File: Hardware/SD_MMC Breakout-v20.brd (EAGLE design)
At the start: 39.4 x 33 mm, 8 parts, among them U1 SD_CARD_SOCKET4UCON

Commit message: Added standoffs, sch work
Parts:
- added FRAME1: FRAME-LETTER, SparkFun-Aesthetics:CREATIVE_COMMONS
- added U$4, U$5: (no value), SparkFun-Electromechanical:STAND-OFF-TIGHT
- U$2: device SparkFun-Aesthetics:CREATIVE_COMMONS -> SparkFun-Aesthetics:CREATIVE_COMMONS@1
- moved JP2 17.8 mm to (19.1, 0.00)
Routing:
- net D2: track 8.53 -> 9.15 mm
- net D3: track 8.53 -> 9.11 mm
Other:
- board size 39.4 x 33 mm -> 39.4 x 35.6 mm
- board text added: "A. Weiss"
- board text added: "Revised by: Patrick Alberts"
- board text added: "v21"
- board text removed: "v20"
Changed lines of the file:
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@@
 <?xml version="1.0" encoding="utf-8"?>
 <!DOCTYPE eagle SYSTEM "eagle.dtd">
-<eagle version="6.4">
+<eagle version="6.5.0">
 <drawing>
 <settings>
@@
 <layer number="106" name="bPlate" color="7" fill="1" visible="no" active="yes"/>
 <layer number="107" name="Crop" color="7" fill="1" visible="no" active="yes"/>
+<layer number="108" name="tplace-old" color="10" fill="1" visible="yes" active="yes"/>
+<layer number="109" name="ref-old" color="11" fill="1" visible="yes" active="yes"/>
 <layer number="116" name="Patch_BOT" color="9" fill="4" visible="no" active="yes"/>
 <layer number="121" name="_tsilk" color="7" fill="1" visible="no" active="yes"/>
@@
 <layer number="144" name="Drill_legend" color="7" fill="1" visible="no" active="yes"/>
 <layer number="151" name="HeatSink" color="7" fill="1" visible="no" active="yes"/>
+<layer number="199" name="Contour" color="7" fill="1" visible="yes" active="yes"/>
 <layer number="200" name="200bmp" color="1" fill="10" visible="no" active="no"/>
 <layer number="201" name="201bmp" color="2" fill="1" visible="no" active="no"/>
@@
 <board>
 <plain>
-<wire x1="0" y1="0" x2="39.37" y2="0" width="0.2032" layer="20"/>
-<wire x1="39.37" y1="0" x2="39.37" y2="33.02" width="0.2032" layer="20"/>
-<wire x1="39.37" y1="33.02" x2="0" y2="33.02" width="0.2032" layer="20"/>
-<wire x1="0" y1="33.02" x2="0" y2="0" width="0.2032" layer="20"/>
+<wire x1="0" y1="-1.27" x2="39.37" y2="-1.27" width="0.2032" layer="20"/>
+<wire x1="39.37" y1="-1.27" x2="39.37" y2="34.29" width="0.2032" layer="20"/>
+<wire x1="39.37" y1="34.29" x2="0" y2="34.29" width="0.2032" layer="20"/>
+<wire x1="0" y1="34.29" x2="0" y2="-1.27" width="0.2032" layer="20"/>
 <text x="2.921" y="14.732" size="1.016" layer="21" ratio="20">VCC</text>
 <text x="38.1" y="10.922" size="1.778" layer="21" ratio="20" rot="R90">SD/MMC</text>
-<text x="38.227" y="19.304" size="1.778" layer="16" font="vector" ratio="15" rot="MR270">v20</text>
+<text x="38.227" y="19.304" size="1.778" layer="16" font="vector" ratio="15" rot="MR270">v21</text>
 <text x="2.921" y="12.192" size="1.016" layer="21" ratio="20">GND</text>
 <text x="2.921" y="9.652" size="1.016" layer="21" ratio="20">D0</text>
@@
 <text x="2.921" y="27.432" size="1.016" layer="21" ratio="20">D2</text>
 <text x="2.921" y="4.572" size="1.016" layer="21" ratio="20">WP</text>
+<text x="24.892" y="-14.351" size="1.778" layer="51">A. Weiss</text>
+<text x="10.287" y="-17.018" size="1.778" layer="51">Revised by: Patrick Alberts</text>
 </plain>
 <attributes>
@@
 <element name="U1" library="SparkFun-Connectors" package="SDCARD_4UCONN" value="SD_CARD_SOCKET4UCON" x="10.16" y="16.51"/>
 <element name="JP1" library="SparkFun-Connectors" package="1X12_HOLES_ONLY" value="M12POGOPIN_HOLES_ONLY" x="6.858" y="2.54" rot="MR90"/>
-<element name="U$2" library="SparkFun-Aesthetics" package="CREATIVE_COMMONS" value="CREATIVE_COMMONS" x="19.05" y="-8.89"/>
+<element name="U$2" library="SparkFun-Aesthetics" package="CREATIVE_COMMONS@1" value="CREATIVE_COMMONS" x="19.05" y="-8.89"/>
 <element name="U$3" library="SparkFun-Aesthetics" package="OSHW-LOGO-S" value="OSHW-LOGOS" x="17.78" y="16.51" rot="MR90"/>
 <element name="JP5" library="SparkFun-Connectors" package="1X10" value="M10&quot;" x="1.27" y="5.08" rot="R90"/>
-<element name="JP2" library="SparkFun" package="MICRO-FIDUCIAL" value="FIDUCIALUFIDUCIAL" x="1.27" y="1.27"/>
+<element name="JP2" library="SparkFun" package="MICRO-FIDUCIAL" value="FIDUCIALUFIDUCIAL" x="19.05" y="0"/>
 <element name="JP3" library="SparkFun" package="MICRO-FIDUCIAL" value="FIDUCIALUFIDUCIAL" x="38.1" y="31.75"/>
+<element name="U$4" library="SparkFun-Electromechanical" package="STAND-OFF-TIGHT" value="" x="2.54" y="31.75"/>
+<element name="U$5" library="SparkFun-Electromechanical" package="STAND-OFF-TIGHT" value="" x="2.54" y="1.27"/>
+<element name="FRAME1" library="SparkFun-Aesthetics" package="CREATIVE_COMMONS" value="FRAME-LETTER" x="-1.50375625" y="-13.97"/>
 </elements>
 <signals>
@@
 <contactref element="U1" pad="3"/>
 <polygon width="0.254" layer="16" isolate="0.3048">
-<vertex x="0" y="33.02"/>
-<vertex x="0" y="0"/>
-<vertex x="39.37" y="0"/>
-<vertex x="39.37" y="33.02"/>
+<vertex x="0" y="34.29"/>
+<vertex x="0" y="-1.27"/>
+<vertex x="39.37" y="-1.27"/>
+<vertex x="39.37" y="34.29"/>
 </polygon>
 <polygon width="0.254" layer="1" isolate="0.3048">
-<vertex x="0" y="33.02"/>
-<vertex x="0" y="0"/>
-<vertex x="39.37" y="0"/>
-<vertex x="39.37" y="33.02"/>
+<vertex x="0" y="34.29"/>
+<vertex x="0" y="-1.27"/>
+<vertex x="39.37" y="-1.27"/>
+<vertex x="39.37" y="34.29"/>
 </polygon>
 <contactref element="U1" pad="6"/>
@@
 <contactref element="U1" pad="9"/>
 <wire x1="9.16" y1="26.4" x2="8.89" y2="26.67" width="0.254" layer="1"/>
-<wire x1="8.89" y1="26.67" x2="3.81" y2="26.67" width="0.254" layer="1"/>
-<wire x1="3.81" y1="26.67" x2="2.54" y2="26.67" width="0.254" layer="1"/>
+<wire x1="8.89" y1="26.67" x2="2.54" y2="26.67" width="0.254" layer="1"/>
 <contactref element="JP5" pad="10"/>
 <wire x1="2.54" y1="26.67" x2="1.27" y2="27.94" width="0.254" layer="1"/>
-<wire x1="9.16" y1="26.4" x2="9.16" y2="25.78" width="0" layer="19" extent="1-1"/>
+<wire x1="9.16" y1="26.4" x2="9.16" y2="25.78" width="0.254" layer="1"/>
 </signal>
 <signal name="D3">
@@
 <wire x1="8.89" y1="24.13" x2="2.54" y2="24.13" width="0.254" layer="1"/>
 <wire x1="2.54" y1="24.13" x2="1.27" y2="25.4" width="0.254" layer="1"/>
-<wire x1="9.16" y1="23.86" x2="9.16" y2="23.28" width="0" layer="19" extent="1-1"/>
+<wire x1="9.16" y1="23.86" x2="9.16" y2="23.28" width="0.254" layer="1"/>
 </signal>
 </signals>

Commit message: Updated Sch
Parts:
- removed U$2: CREATIVE_COMMONS, SparkFun-Aesthetics:CREATIVE_COMMONS@1
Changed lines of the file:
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@@
 <element name="U1" library="SparkFun-Connectors" package="SDCARD_4UCONN" value="SD_CARD_SOCKET4UCON" x="10.16" y="16.51"/>
 <element name="JP1" library="SparkFun-Connectors" package="1X12_HOLES_ONLY" value="M12POGOPIN_HOLES_ONLY" x="6.858" y="2.54" rot="MR90"/>
-<element name="U$2" library="SparkFun-Aesthetics" package="CREATIVE_COMMONS@1" value="CREATIVE_COMMONS" x="19.05" y="-8.89"/>
 <element name="U$3" library="SparkFun-Aesthetics" package="OSHW-LOGO-S" value="OSHW-LOGOS" x="17.78" y="16.51" rot="MR90"/>
 <element name="JP5" library="SparkFun-Connectors" package="1X10" value="M10&quot;" x="1.27" y="5.08" rot="R90"/>

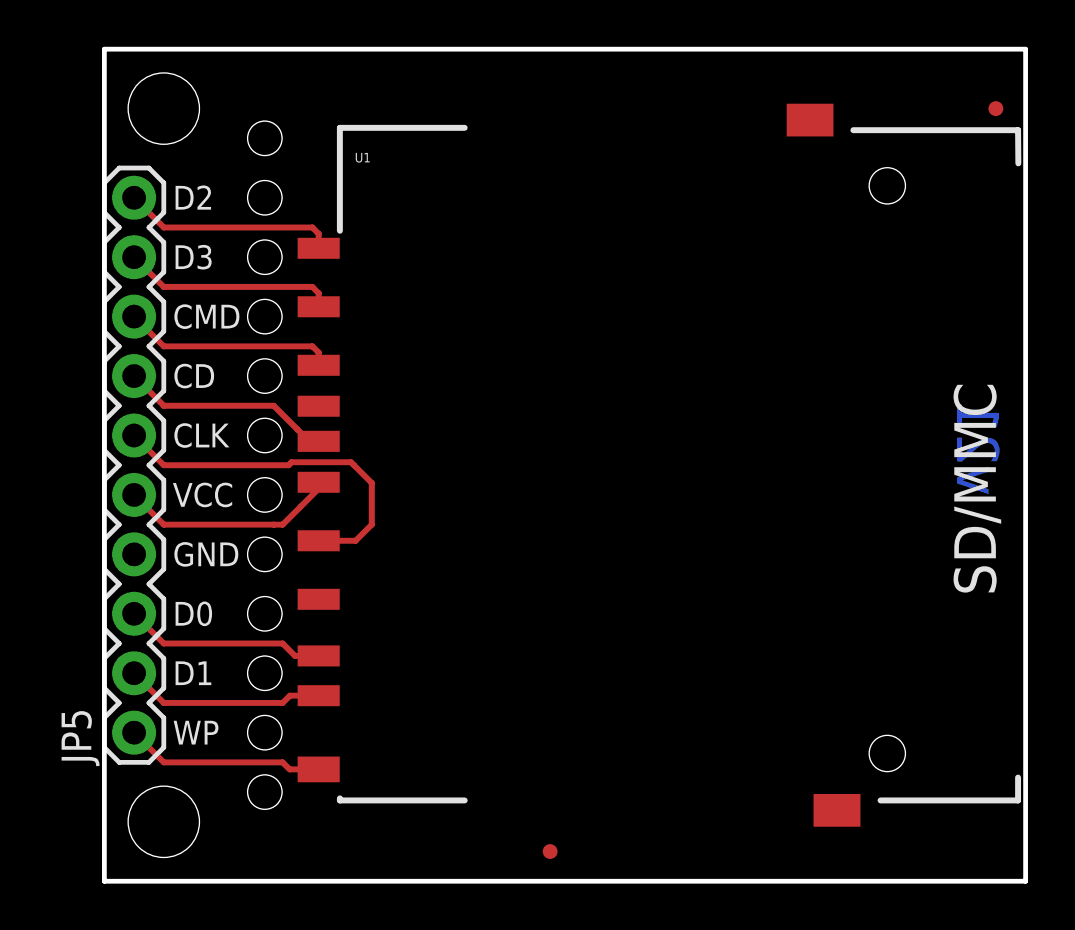
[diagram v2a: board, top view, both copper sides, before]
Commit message: added new sd socket
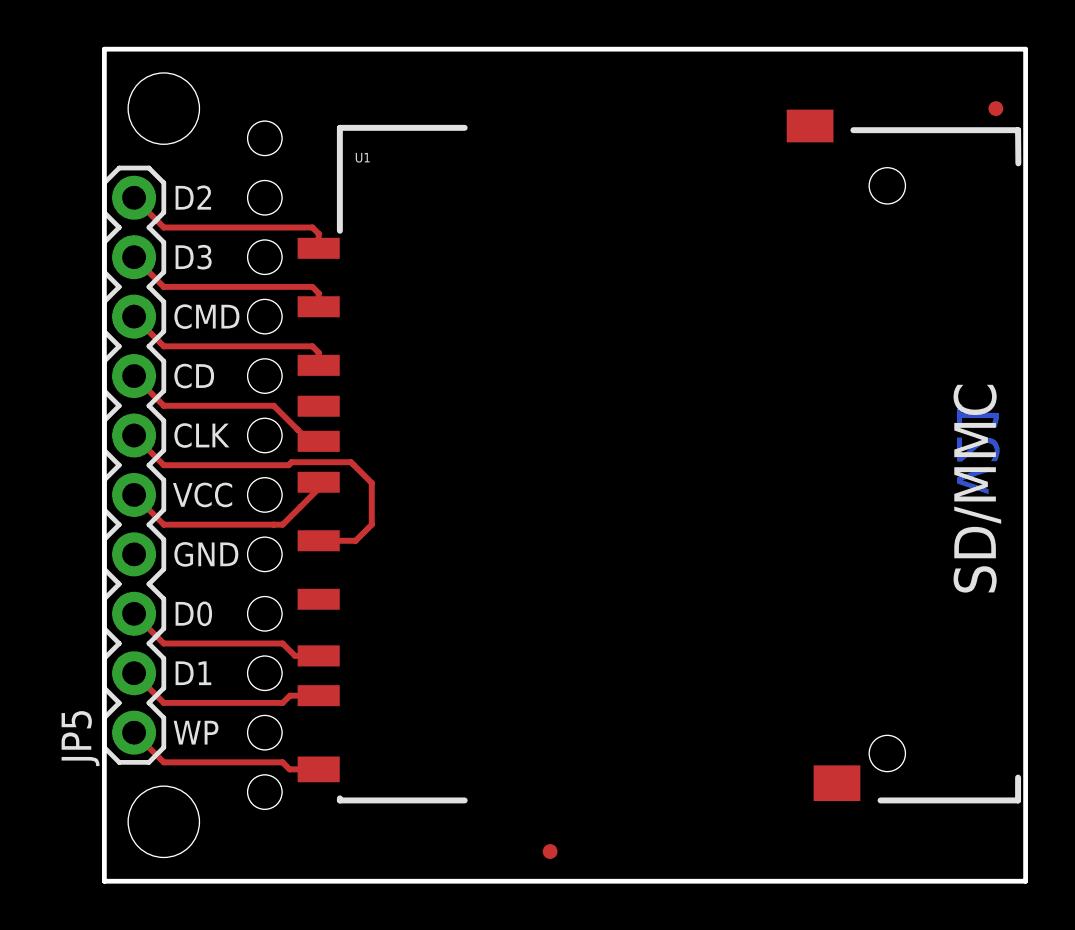
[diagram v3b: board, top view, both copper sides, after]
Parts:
- U1: value SD_CARD_SOCKET4UCON -> SD_CARD_SOCKET; device SparkFun-Connectors:SDCARD_4UCONN -> SparkFun-Connectors:SD_1:1
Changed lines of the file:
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@@
 <?xml version="1.0" encoding="utf-8"?>
 <!DOCTYPE eagle SYSTEM "eagle.dtd">
-<eagle version="6.5.0">
+<eagle version="6.4">
 <drawing>
 <settings>
@@
 <layer number="18" name="Vias" color="2" fill="1" visible="yes" active="yes"/>
 <layer number="19" name="Unrouted" color="6" fill="1" visible="yes" active="yes"/>
-<layer number="20" name="Dimension" color="6" fill="1" visible="yes" active="yes"/>
+<layer number="20" name="Dimension" color="15" fill="1" visible="yes" active="yes"/>
 <layer number="21" name="tPlace" color="16" fill="1" visible="yes" active="yes"/>
 <layer number="22" name="bPlace" color="14" fill="1" visible="yes" active="yes"/>
@@
 <layer number="106" name="bPlate" color="7" fill="1" visible="no" active="yes"/>
 <layer number="107" name="Crop" color="7" fill="1" visible="no" active="yes"/>
-<layer number="108" name="tplace-old" color="10" fill="1" visible="yes" active="yes"/>
-<layer number="109" name="ref-old" color="11" fill="1" visible="yes" active="yes"/>
+<layer number="108" name="tplace-old" color="10" fill="1" visible="no" active="yes"/>
+<layer number="109" name="ref-old" color="11" fill="1" visible="no" active="yes"/>
+<layer number="110" name="fp0" color="7" fill="1" visible="yes" active="yes"/>
+<layer number="111" name="LPC17xx" color="7" fill="1" visible="yes" active="yes"/>
+<layer number="112" name="tSilk" color="7" fill="1" visible="yes" active="yes"/>
+<layer number="113" name="IDFDebug" color="4" fill="1" visible="yes" active="yes"/>
 <layer number="116" name="Patch_BOT" color="9" fill="4" visible="no" active="yes"/>
 <layer number="121" name="_tsilk" color="7" fill="1" visible="no" active="yes"/>
 <layer number="122" name="_bsilk" color="7" fill="1" visible="no" active="yes"/>
+<layer number="123" name="tTestmark" color="7" fill="1" visible="yes" active="yes"/>
+<layer number="124" name="bTestmark" color="7" fill="1" visible="yes" active="yes"/>
 <layer number="125" name="_tNames" color="7" fill="1" visible="no" active="yes"/>
+<layer number="126" name="_bNames" color="7" fill="1" visible="yes" active="yes"/>
+<layer number="127" name="_tValues" color="7" fill="1" visible="yes" active="yes"/>
+<layer number="128" name="_bValues" color="7" fill="1" visible="yes" active="yes"/>
+<layer number="131" name="tAdjust" color="7" fill="1" visible="yes" active="yes"/>
+<layer number="132" name="bAdjust" color="7" fill="1" visible="yes" active="yes"/>
 <layer number="144" name="Drill_legend" color="7" fill="1" visible="no" active="yes"/>
 <layer number="151" name="HeatSink" color="7" fill="1" visible="no" active="yes"/>
-<layer number="199" name="Contour" color="7" fill="1" visible="yes" active="yes"/>
+<layer number="152" name="_bDocu" color="7" fill="1" visible="yes" active="yes"/>
+<layer number="199" name="Contour" color="7" fill="1" visible="no" active="yes"/>
 <layer number="200" name="200bmp" color="1" fill="10" visible="no" active="no"/>
 <layer number="201" name="201bmp" color="2" fill="1" visible="no" active="no"/>
@@
 <layer number="223" name="223bmp" color="24" fill="1" visible="no" active="no"/>
 <layer number="224" name="224bmp" color="25" fill="1" visible="no" active="no"/>
+<layer number="248" name="Housing" color="7" fill="1" visible="yes" active="yes"/>
+<layer number="249" name="Edge" color="7" fill="1" visible="yes" active="yes"/>
 <layer number="250" name="Descript" color="3" fill="1" visible="no" active="no"/>
 <layer number="251" name="SMDround" color="12" fill="11" visible="no" active="no"/>
@@
 <elements>
 <element name="U$1" library="SparkFun" package="SFE-NEW-WEBLOGO" value="LOGO-SFENEW" x="19.05" y="6.3246" rot="MR90"/>
-<element name="U1" library="SparkFun-Connectors" package="SDCARD_4UCONN" value="SD_CARD_SOCKET4UCON" x="10.16" y="16.51"/>
+<element name="U1" library="SparkFun-Connectors" package="SD_1:1" value="SD_CARD_SOCKET" x="10.16" y="16.51"/>
 <element name="JP1" library="SparkFun-Connectors" package="1X12_HOLES_ONLY" value="M12POGOPIN_HOLES_ONLY" x="6.858" y="2.54" rot="MR90"/>
 <element name="U$3" library="SparkFun-Aesthetics" package="OSHW-LOGO-S" value="OSHW-LOGOS" x="17.78" y="16.51" rot="MR90"/>

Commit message: Changed Font, Removed Extra Pins
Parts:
- removed JP1: M12POGOPIN_HOLES_ONLY, SparkFun-Connectors:1X12_HOLES_ONLY
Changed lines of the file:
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@@
 <layer number="108" name="tplace-old" color="10" fill="1" visible="no" active="yes"/>
 <layer number="109" name="ref-old" color="11" fill="1" visible="no" active="yes"/>
-<layer number="110" name="fp0" color="7" fill="1" visible="yes" active="yes"/>
-<layer number="111" name="LPC17xx" color="7" fill="1" visible="yes" active="yes"/>
-<layer number="112" name="tSilk" color="7" fill="1" visible="yes" active="yes"/>
-<layer number="113" name="IDFDebug" color="4" fill="1" visible="yes" active="yes"/>
+<layer number="110" name="fp0" color="7" fill="1" visible="no" active="yes"/>
+<layer number="111" name="LPC17xx" color="7" fill="1" visible="no" active="yes"/>
+<layer number="112" name="tSilk" color="7" fill="1" visible="no" active="yes"/>
+<layer number="113" name="IDFDebug" color="4" fill="1" visible="no" active="yes"/>
 <layer number="116" name="Patch_BOT" color="9" fill="4" visible="no" active="yes"/>
 <layer number="121" name="_tsilk" color="7" fill="1" visible="no" active="yes"/>
 <layer number="122" name="_bsilk" color="7" fill="1" visible="no" active="yes"/>
-<layer number="123" name="tTestmark" color="7" fill="1" visible="yes" active="yes"/>
-<layer number="124" name="bTestmark" color="7" fill="1" visible="yes" active="yes"/>
+<layer number="123" name="tTestmark" color="7" fill="1" visible="no" active="yes"/>
+<layer number="124" name="bTestmark" color="7" fill="1" visible="no" active="yes"/>
 <layer number="125" name="_tNames" color="7" fill="1" visible="no" active="yes"/>
-<layer number="126" name="_bNames" color="7" fill="1" visible="yes" active="yes"/>
-<layer number="127" name="_tValues" color="7" fill="1" visible="yes" active="yes"/>
-<layer number="128" name="_bValues" color="7" fill="1" visible="yes" active="yes"/>
-<layer number="131" name="tAdjust" color="7" fill="1" visible="yes" active="yes"/>
-<layer number="132" name="bAdjust" color="7" fill="1" visible="yes" active="yes"/>
+<layer number="126" name="_bNames" color="7" fill="1" visible="no" active="yes"/>
+<layer number="127" name="_tValues" color="7" fill="1" visible="no" active="yes"/>
+<layer number="128" name="_bValues" color="7" fill="1" visible="no" active="yes"/>
+<layer number="131" name="tAdjust" color="7" fill="1" visible="no" active="yes"/>
+<layer number="132" name="bAdjust" color="7" fill="1" visible="no" active="yes"/>
 <layer number="144" name="Drill_legend" color="7" fill="1" visible="no" active="yes"/>
 <layer number="151" name="HeatSink" color="7" fill="1" visible="no" active="yes"/>
-<layer number="152" name="_bDocu" color="7" fill="1" visible="yes" active="yes"/>
+<layer number="152" name="_bDocu" color="7" fill="1" visible="no" active="yes"/>
 <layer number="199" name="Contour" color="7" fill="1" visible="no" active="yes"/>
 <layer number="200" name="200bmp" color="1" fill="10" visible="no" active="no"/>
@@
 <layer number="223" name="223bmp" color="24" fill="1" visible="no" active="no"/>
 <layer number="224" name="224bmp" color="25" fill="1" visible="no" active="no"/>
-<layer number="248" name="Housing" color="7" fill="1" visible="yes" active="yes"/>
-<layer number="249" name="Edge" color="7" fill="1" visible="yes" active="yes"/>
+<layer number="248" name="Housing" color="7" fill="1" visible="no" active="yes"/>
+<layer number="249" name="Edge" color="7" fill="1" visible="no" active="yes"/>
 <layer number="250" name="Descript" color="3" fill="1" visible="no" active="no"/>
 <layer number="251" name="SMDround" color="12" fill="11" visible="no" active="no"/>
@@
 <wire x1="39.37" y1="34.29" x2="0" y2="34.29" width="0.2032" layer="20"/>
 <wire x1="0" y1="34.29" x2="0" y2="-1.27" width="0.2032" layer="20"/>
-<text x="2.921" y="14.732" size="1.016" layer="21" ratio="20">VCC</text>
+<text x="2.921" y="14.732" size="1.016" layer="21" font="vector" ratio="15">VCC</text>
 <text x="38.1" y="10.922" size="1.778" layer="21" ratio="20" rot="R90">SD/MMC</text>
 <text x="38.227" y="19.304" size="1.778" layer="16" font="vector" ratio="15" rot="MR270">v21</text>
-<text x="2.921" y="12.192" size="1.016" layer="21" ratio="20">GND</text>
-<text x="2.921" y="9.652" size="1.016" layer="21" ratio="20">D0</text>
-<text x="2.921" y="7.112" size="1.016" layer="21" ratio="20">D1</text>
-<text x="2.921" y="17.272" size="1.016" layer="21" ratio="20">CLK</text>
-<text x="2.921" y="19.812" size="1.016" layer="21" ratio="20">CD</text>
-<text x="2.921" y="22.352" size="1.016" layer="21" ratio="20">CMD</text>
-<text x="2.921" y="24.892" size="1.016" layer="21" ratio="20">D3</text>
-<text x="2.921" y="27.432" size="1.016" layer="21" ratio="20">D2</text>
-<text x="2.921" y="4.572" size="1.016" layer="21" ratio="20">WP</text>
+<text x="2.921" y="12.192" size="1.016" layer="21" font="vector" ratio="15">GND</text>
+<text x="2.921" y="9.652" size="1.016" layer="21" font="vector" ratio="15">D0</text>
+<text x="2.921" y="7.112" size="1.016" layer="21" font="vector" ratio="15">D1</text>
+<text x="2.921" y="17.272" size="1.016" layer="21" font="vector" ratio="15">CLK</text>
+<text x="2.921" y="19.812" size="1.016" layer="21" font="vector" ratio="15">CD</text>
+<text x="2.921" y="22.352" size="1.016" layer="21" font="vector" ratio="15">CMD</text>
+<text x="2.921" y="24.892" size="1.016" layer="21" font="vector" ratio="15">D3</text>
+<text x="2.921" y="27.432" size="1.016" layer="21" font="vector" ratio="15">D2</text>
+<text x="2.921" y="4.572" size="1.016" layer="21" font="vector" ratio="15">WP</text>
 <text x="24.892" y="-14.351" size="1.778" layer="51">A. Weiss</text>
 <text x="10.287" y="-17.018" size="1.778" layer="51">Revised by: Patrick Alberts</text>
@@
 <element name="U$1" library="SparkFun" package="SFE-NEW-WEBLOGO" value="LOGO-SFENEW" x="19.05" y="6.3246" rot="MR90"/>
 <element name="U1" library="SparkFun-Connectors" package="SD_1:1" value="SD_CARD_SOCKET" x="10.16" y="16.51"/>
-<element name="JP1" library="SparkFun-Connectors" package="1X12_HOLES_ONLY" value="M12POGOPIN_HOLES_ONLY" x="6.858" y="2.54" rot="MR90"/>
 <element name="U$3" library="SparkFun-Aesthetics" package="OSHW-LOGO-S" value="OSHW-LOGOS" x="17.78" y="16.51" rot="MR90"/>
 <element name="JP5" library="SparkFun-Connectors" package="1X10" value="M10&quot;" x="1.27" y="5.08" rot="R90"/>

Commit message: changed fiducial to regular size
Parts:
- removed JP2, JP3: FIDUCIALUFIDUCIAL, SparkFun:MICRO-FIDUCIAL
- added FID1, FID2: FIDUCIAL1X2, SparkFun-Aesthetics:FIDUCIAL-1X2
